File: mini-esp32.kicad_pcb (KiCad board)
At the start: 4 copper layers, 29 x 58 mm, 46 parts, among them J1 BAT, J2 USB_B_Micro, J5 Conn_01x18, J6 Conn_01x18, Q1 AO3401A, Q2 S8050, Q3 S8050, Q4 2N7002, SW1 RESET, U1 ESP32-WROOM-32D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

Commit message: Rename files
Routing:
- net I35: track 44.7 -> 45.4 mm

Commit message: Fix power/gnd planes in the antenna zone.
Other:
- board text added: "Mini ESP32 V2.0.1"
- board text removed: "Mini ESP32 V2.0"
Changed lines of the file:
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@@
       (drillshape 0)
       (scaleselection 1)
-      (outputdirectory "gerber/"))
+      (outputdirectory "output/"))
   )
   (net 0 "")
@@
       (effects (font (size 0.8 0.8) (thickness 0.12)))
     )
-    (pad 2 smd roundrect (at 1.4625 0) (size 1.125 1.75) (layers F.Cu F.Paste F.Mask) (roundrect_rratio 0.2222213333333333)
+    (pad 2 smd roundrect (at 1.4625 0) (size 1.125 1.75) (layers F.Cu F.Paste F.Mask) (roundrect_rratio 0.2222204444444444)
       (net 12 VBUS))
-    (pad 1 smd roundrect (at -1.4625 0) (size 1.125 1.75) (layers F.Cu F.Paste F.Mask) (roundrect_rratio 0.2222213333333333)
+    (pad 1 smd roundrect (at -1.4625 0) (size 1.125 1.75) (layers F.Cu F.Paste F.Mask) (roundrect_rratio 0.2222204444444444)
       (net 1 "Net-(C1-Pad1)"))
     (model ${KISYS3DMOD}/Resistor_SMD.3dshapes/R_1206_3216Metric.wrl
@@
     (effects (font (size 0.8 0.8) (thickness 0.15)))
   )
-  (gr_text "Mini ESP32\nV2.0" (at 133.4 91 270) (layer B.SilkS)
+  (gr_text "Mini ESP32\nV2.0.1" (at 133.4 91 270) (layer B.SilkS)
     (effects (font (size 4 4) (thickness 0.75)) (justify mirror))
   )
@@
     (polygon
       (pts
-        (xy 149 120.5) (xy 118.5 120.5) (xy 118.5 61) (xy 149 61)
+        (xy 149 127.1) (xy 118.5 127.1) (xy 118.5 67.6) (xy 149 67.6)
       )
     )
@@
     (polygon
       (pts
-        (xy 149 120.5) (xy 118.5 120.5) (xy 118.5 61) (xy 149 61)
+        (xy 149 127.1) (xy 118.5 127.1) (xy 118.5 67.6) (xy 149 67.6)
       )
     )

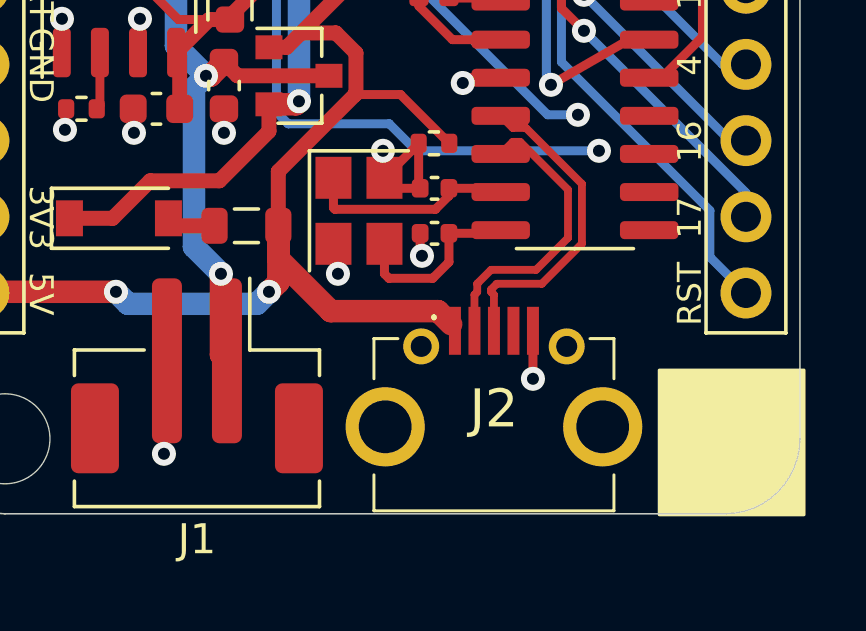
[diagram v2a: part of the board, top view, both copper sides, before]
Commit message: Fix USB Micro B footprint to official one
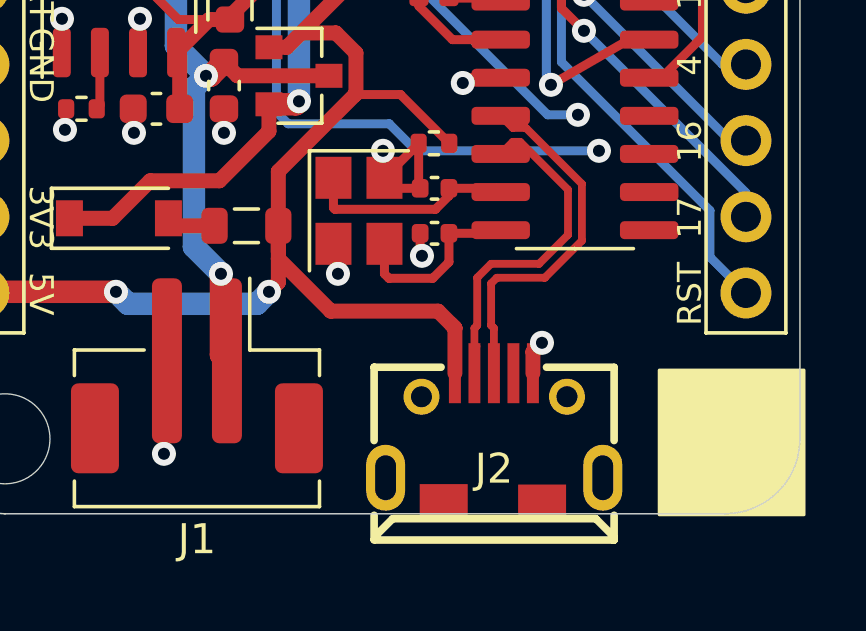
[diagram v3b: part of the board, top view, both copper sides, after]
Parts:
- J2: footprint serialx:C10418 -> LCSC:USB_Micro-B_Jing-C10418-A01SB141B1-067
- U1: value ESP32-WROOM-32D -> ESP32-WROOM-32E
- moved J2 1.10 mm to (138.0, 117.6), turned to 0 degrees
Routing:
- net UD-: track 9.94 -> 12.4 mm
- net UD+: track 10.7 -> 13.1 mm
- net VBUS: track 48.6 -> 49.4 mm

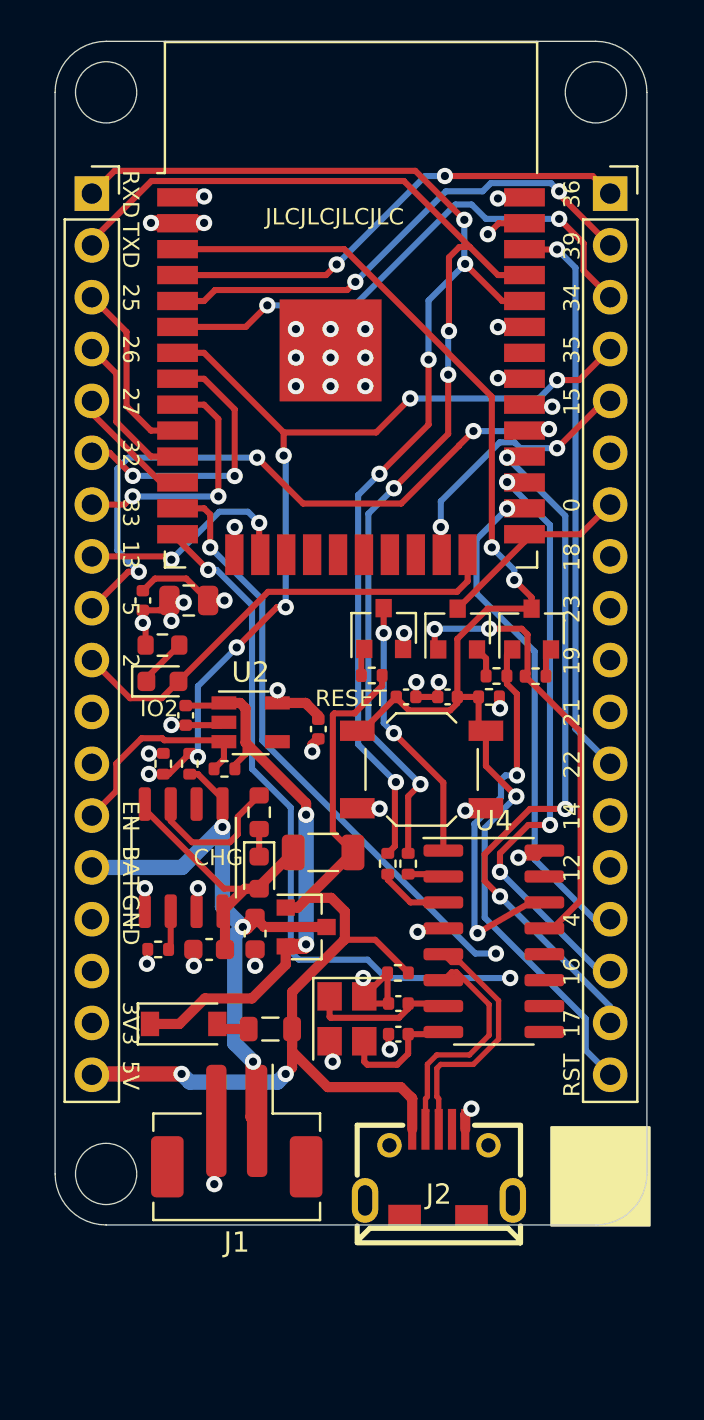
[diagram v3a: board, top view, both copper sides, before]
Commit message: Pad courtyard adjustment. ESP32 GND pad larger hole. Etc. V2.0.1
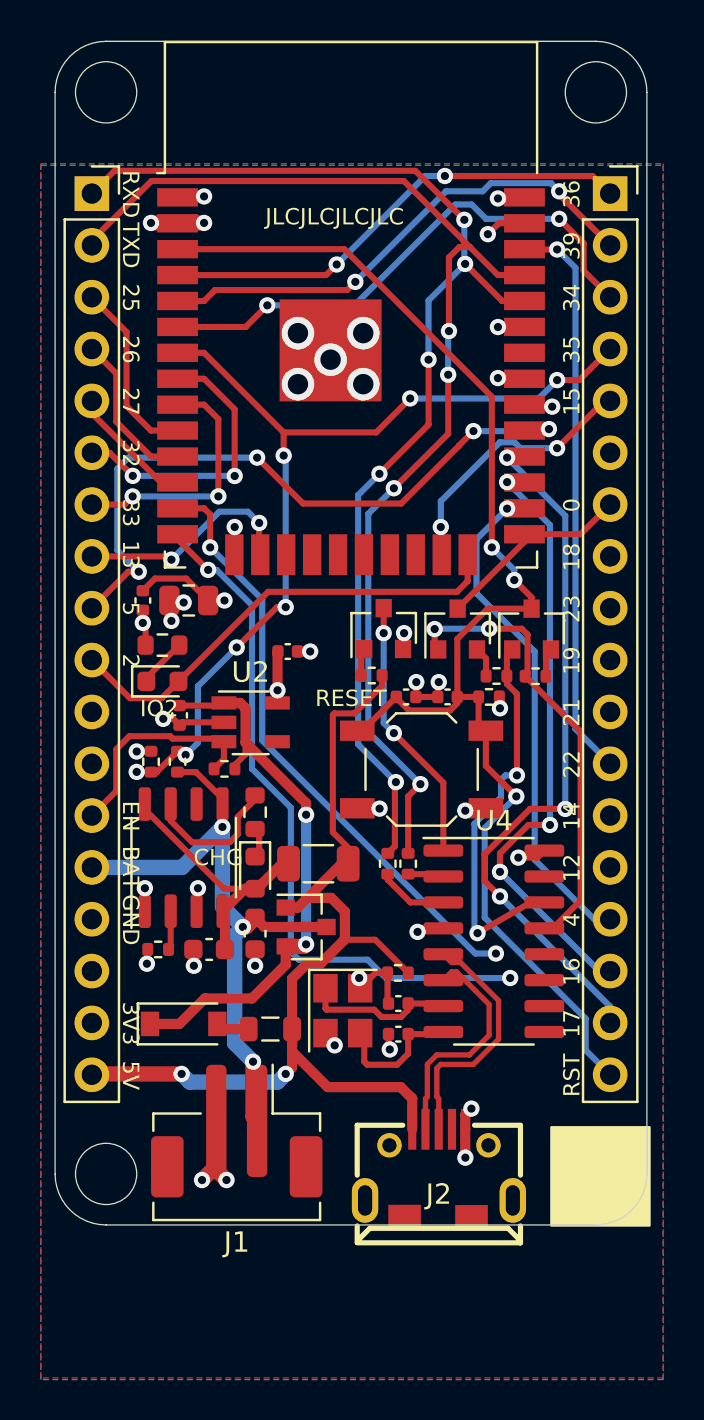
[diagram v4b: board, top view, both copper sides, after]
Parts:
- moved C6 10.7 mm to (123.5, 89.0)
- moved C3 7.53 mm to (130.6, 91.5), turned to 0 degrees
- moved R5 0.61 mm to (125.2, 96.9)
- moved R6 0.61 mm to (123.9, 96.9)
- moved R2 0.60 mm to (132.1, 101.9)
- moved Y1 0.45 mm to (133.3, 109.1)
- moved C2 0.30 mm to (125.3, 94.6)
- moved D2 0.20 mm to (129.0, 102.3)
- moved R4 0.20 mm to (129.0, 99.4)
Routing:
- net VDD: track 13.9 -> 13.2 mm
- net +BATT: track 30.6 -> 31.3 mm
- net Net-(C9-Pad1): track 7.12 -> 7.74 mm
- net EN: track 11.1 -> 11.7 mm
- net GND: track 34.9 -> 35.3 mm, vias 33 -> 31
- added copper zone on B.Cu, net GND
- added copper zone on F.Cu, net GND

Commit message: Improved routing. Internal layers are not used anymore for routing.
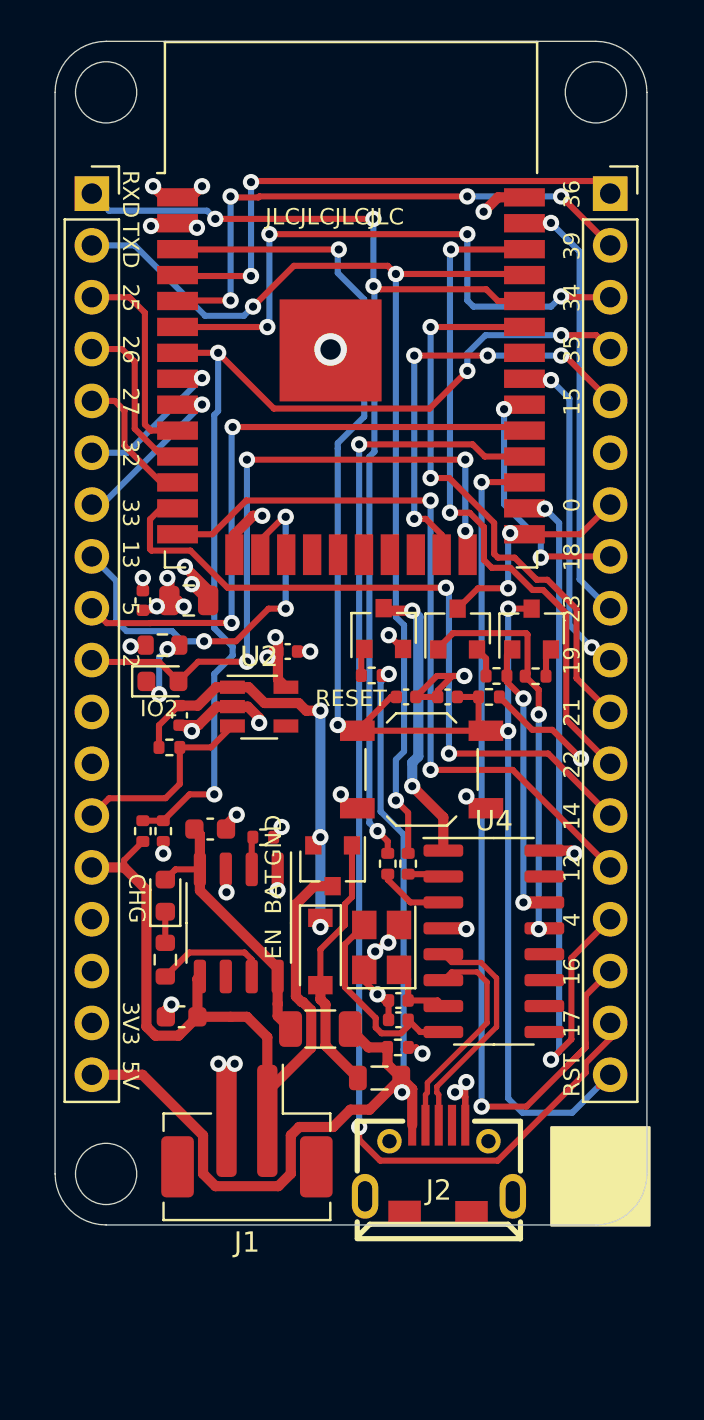
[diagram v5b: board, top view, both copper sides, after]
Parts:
- moved R4 8.46 mm to (124.6, 106.6), turned to 90 degrees
- moved R2 8.10 mm to (132.2, 110.0)
- moved D1 7.58 mm to (132.2, 106.2), turned to 270 degrees
- moved R9 7.53 mm to (129.4, 100.6), turned to 180 degrees
- moved C1 5.90 mm to (126.8, 100.2), turned to 0 degrees
- moved FB1 5.86 mm to (135.1, 112.4)
- moved C5 5.44 mm to (125.4, 109.4), turned to 180 degrees
- moved D2 4.54 mm to (124.6, 103.5), turned to 90 degrees
- moved U3 4.19 mm to (128.2, 104.8), turned to 270 degrees
- moved R5 3.80 mm to (123.5, 100.3)
- moved R1 3.65 mm to (136.0, 110.9), turned to 0 degrees
- moved Y1 3.64 mm to (135.2, 106.0), turned to 90 degrees
- moved R6 3.45 mm to (124.5, 100.3), turned to 270 degrees
- moved Q1 3.27 mm to (132.8, 102.0), turned to 270 degrees
- moved R3 2.90 mm to (124.8, 96.2), turned to 0 degrees
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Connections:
- Q1 pad 1: VBUS -> Net-(D1-Pad2)
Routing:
- net IO17: track 35.0 -> 59.4 mm, vias 3 -> 2
- net IO16: track 29.9 -> 44.5 mm, vias 3 -> 2
- net IO4: track 24.8 -> 37.0 mm, vias 1 -> 2
- net RESET: track 66.5 -> 78.3 mm, vias 3 -> 4
- net GND: track 35.3 -> 46.8 mm, vias 31 -> 30
- net Net-(D1-Pad2): track 1.64 -> 12.8 mm
- net IO2: track 22.9 -> 33.7 mm, vias 0 -> 4
- net IO13: track 11.0 -> 20.0 mm, vias 2 -> 3
- net IO15: track 13.2 -> 21.2 mm, vias 2 -> 4
- net +BATT: track 31.3 -> 38.6 mm, vias 3 -> 0
- net IO32: track 14.2 -> 8.13 mm, vias 2 -> 1
- net IO14: track 41.4 -> 35.7 mm
- net Net-(C2-Pad1): track 27.5 -> 21.8 mm, vias 2 -> 3
- net IO22: track 27.9 -> 33.5 mm, vias 1 -> 2
- net I35: track 45.5 -> 51.1 mm, vias 7 -> 4
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- removed copper zone on B.Cu, net GND
- removed copper zone on F.Cu, net GND

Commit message: Add FS312F-G battery protection IC
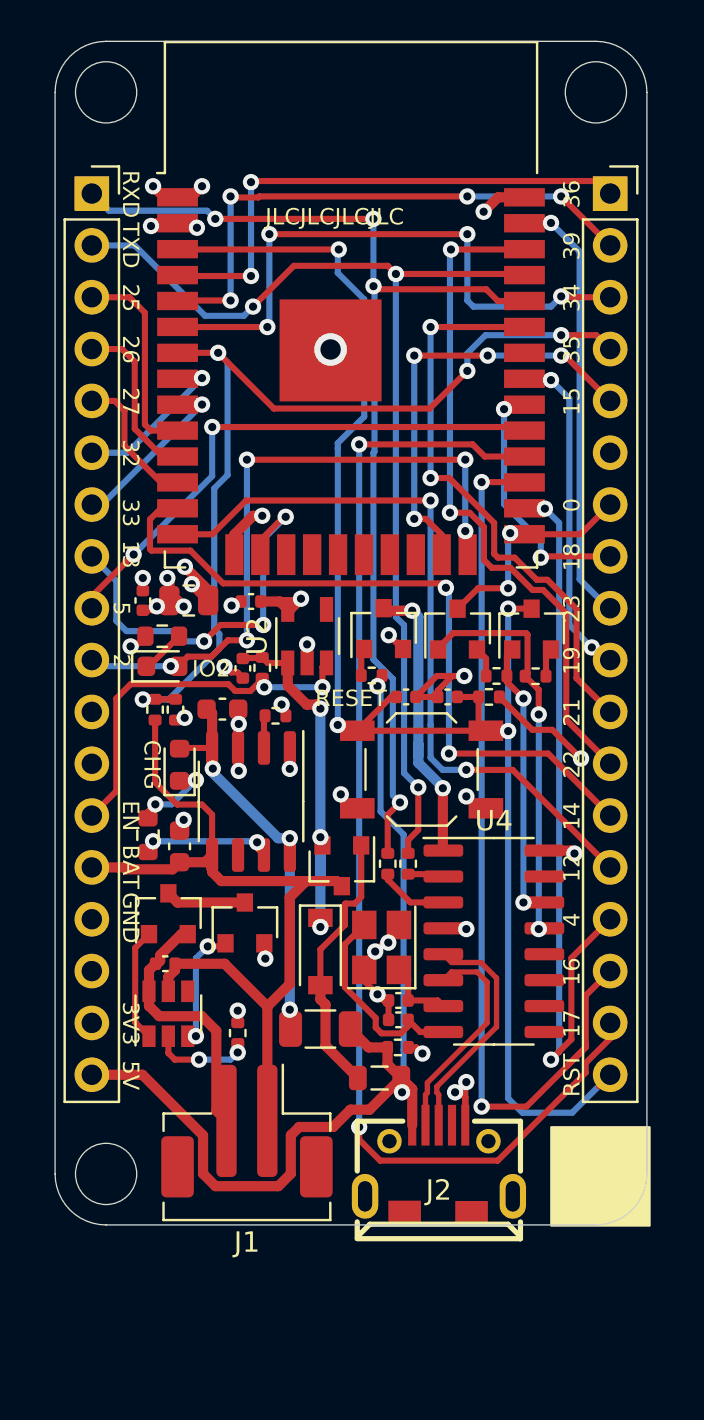
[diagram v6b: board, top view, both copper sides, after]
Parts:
- added C11: 100n, Capacitor_SMD:C_0402_1005Metric, F.Cu at (124.6, 106.8)
- added Q5: AO3400A, Package_TO_SOT_SMD:SOT-23, F.Cu at (124.8, 104.3)
- added Q6: AO3400A, Package_TO_SOT_SMD:SOT-23, F.Cu at (128.5, 104.8)
- added R15: 2k, Resistor_SMD:R_0402_1005Metric, F.Cu at (128.2, 110.2)
- added U5: FS312F-G, Package_TO_SOT_SMD:SOT-23-6, F.Cu at (124.8, 109.2)
- moved C5 8.35 mm to (125.3, 101.0), turned to 90 degrees
- moved D2 6.45 mm to (125.3, 97.0)
- moved R4 6.16 mm to (123.8, 100.5)
- moved R3 5.99 mm to (129.3, 92.3), turned to 270 degrees
- moved U3 5.98 mm to (128.8, 98.8)
- moved R5 5.98 mm to (124.1, 94.3)
- moved R6 5.98 mm to (125.1, 94.3)
- moved R9 5.98 mm to (130.0, 94.7)
- moved C1 5.91 mm to (127.4, 94.3)
- moved U2 4.17 mm to (131.6, 90.8), turned to 90 degrees
- moved C2 3.86 mm to (128.4, 92.3)
- moved C3 3.04 mm to (128.8, 89.0), turned to 180 degrees
- moved D3 0.74 mm to (124.5, 92.2)
- moved Q1 0.45 mm to (133.2, 102.0)
- moved R11 0.44 mm to (124.5, 90.8)
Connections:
- net +BATT renamed BAT+
- J1 pad 2: GND -> BAT-
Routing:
- net BAT-: track 0.00 -> 13.0 mm
- net EN: track 9.76 -> 18.7 mm, vias 0 -> 2
- net Net-(Q6-Pad1): track 0.00 -> 5.97 mm, vias 0 -> 2
- net Net-(C1-Pad1): track 13.7 -> 19.4 mm, vias 0 -> 3
- net Net-(Q5-Pad1): track 0.00 -> 5.56 mm
- net I35: track 51.1 -> 46.0 mm
- net Net-(R15-Pad1): track 0.00 -> 4.95 mm, vias 0 -> 2
- net GND: track 46.8 -> 42.2 mm
- net IO5: track 31.1 -> 26.7 mm
- net BAT+: track 38.6 -> 43.0 mm
- net Net-(Q5-Pad3): track 0.00 -> 3.94 mm
- net Net-(D2-Pad1): track 1.53 -> 4.13 mm, vias 0 -> 2
- net Net-(C2-Pad1): track 21.8 -> 19.3 mm
- net Net-(D3-Pad1): track 3.94 -> 2.20 mm, vias 2 -> 0
- net IO2: track 33.7 -> 32.7 mm, vias 4 -> 5
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
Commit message: Polishing. V2.1.0
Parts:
- moved C6 0.80 mm to (123.5, 88.2)
- moved U5 0.55 mm to (125.3, 109.2)
- moved Q5 0.50 mm to (125.2, 104.3)
- moved C3 0.45 mm to (128.8, 89.5)
- moved Q6 0.35 mm to (128.8, 104.8)
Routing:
- net BAT-: track 13.0 -> 16.0 mm
- net Net-(Q5-Pad1): track 5.56 -> 7.26 mm, vias 0 -> 2
- net VDD: track 16.6 -> 17.7 mm, vias 9 -> 10
- net Net-(R15-Pad1): track 4.95 -> 4.36 mm
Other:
- board text added: "Mini ESP32 V2.1.0"
- board text removed: "2"
- board text removed: "Mini ESP32 V2.0.1"

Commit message: Fix three critical bugs
1. Fix RXD TXD wiring
2. Fix LDO EN pin resistor
3. Fix programming not working (DTR RTS programming transistor resistor values)
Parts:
- removed R12, R13: 2.4k, Resistor_SMD:R_0402_1005Metric
- removed R3: 100k, Resistor_SMD:R_0402_1005Metric
- R7, R8: value 10k -> 1k
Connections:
- C2 pad 1: Net-(C2-Pad1) -> EN
- D1 pad 1: Net-(C2-Pad1) -> EN
- Q1 pad 2: Net-(C2-Pad1) -> EN
- U2 pad 1: Net-(C2-Pad1) -> EN
- U4 pad 2: Net-(R12-Pad1) -> RXD0
- U4 pad 3: Net-(R13-Pad2) -> TXD0
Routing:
- net EN: track 18.7 -> 39.0 mm, vias 2 -> 5
- net Net-(C2-Pad1): track 19.3 -> 0.00 mm, vias 3 -> 0
- net TXD0: track 53.0 -> 57.8 mm
- net Net-(R13-Pad2): track 3.46 -> 0.00 mm
- net RXD0: track 53.9 -> 57.0 mm
- net Net-(R12-Pad1): track 1.77 -> 0.00 mm
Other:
- board text added: "Mini ESP32 V3.0"
- board text removed: "Mini ESP32 V2.1.0"
